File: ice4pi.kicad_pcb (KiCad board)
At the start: 4 copper layers, 85 x 56 mm, 41 parts, among them J1 Conn_02x03, J2 Raspberry_Pi_2_3, J3 USB_C_Receptacle_USB2.0, J4 RJ45_Abracon_ARJP11A-MASA-B-A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, U1 ENC28J60x-SS, U2 DSC1001DE1-025.0000, U3 TPS2375-1

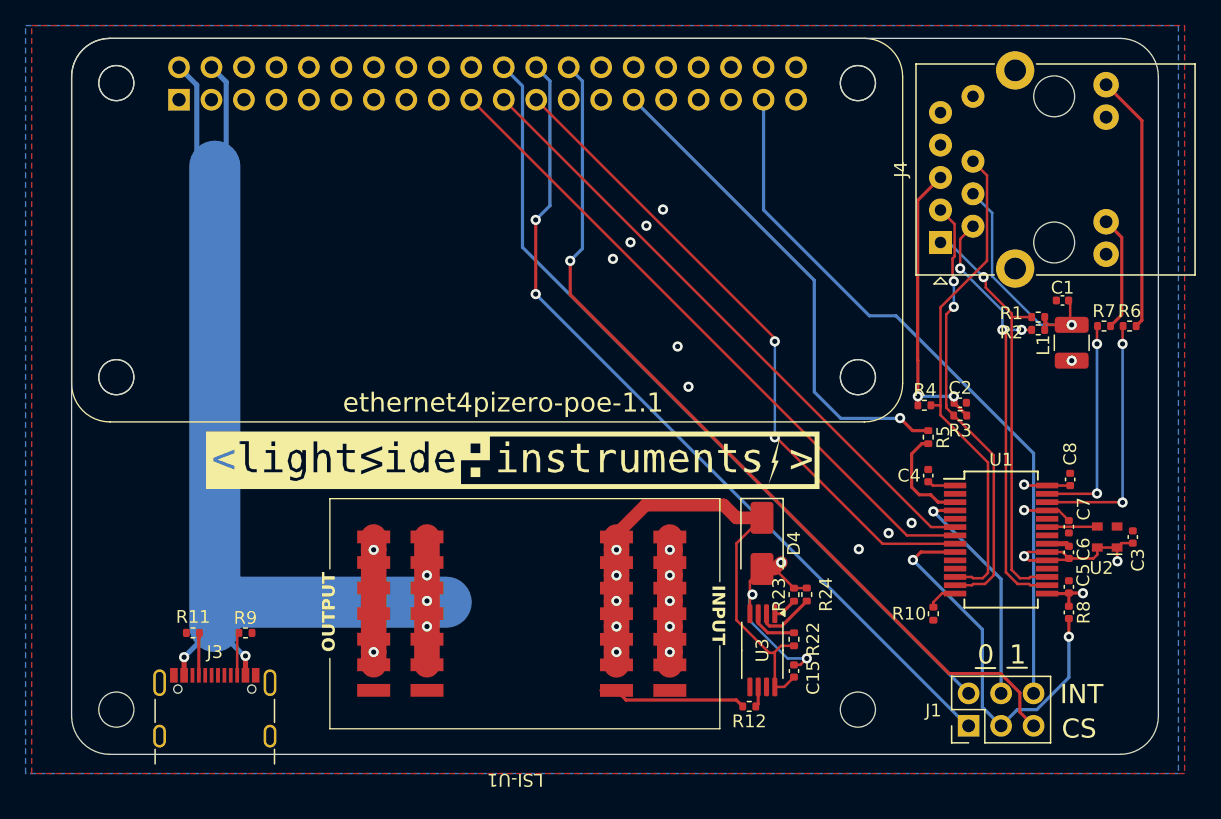
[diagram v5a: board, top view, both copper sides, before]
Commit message: feat: fixed led polarity
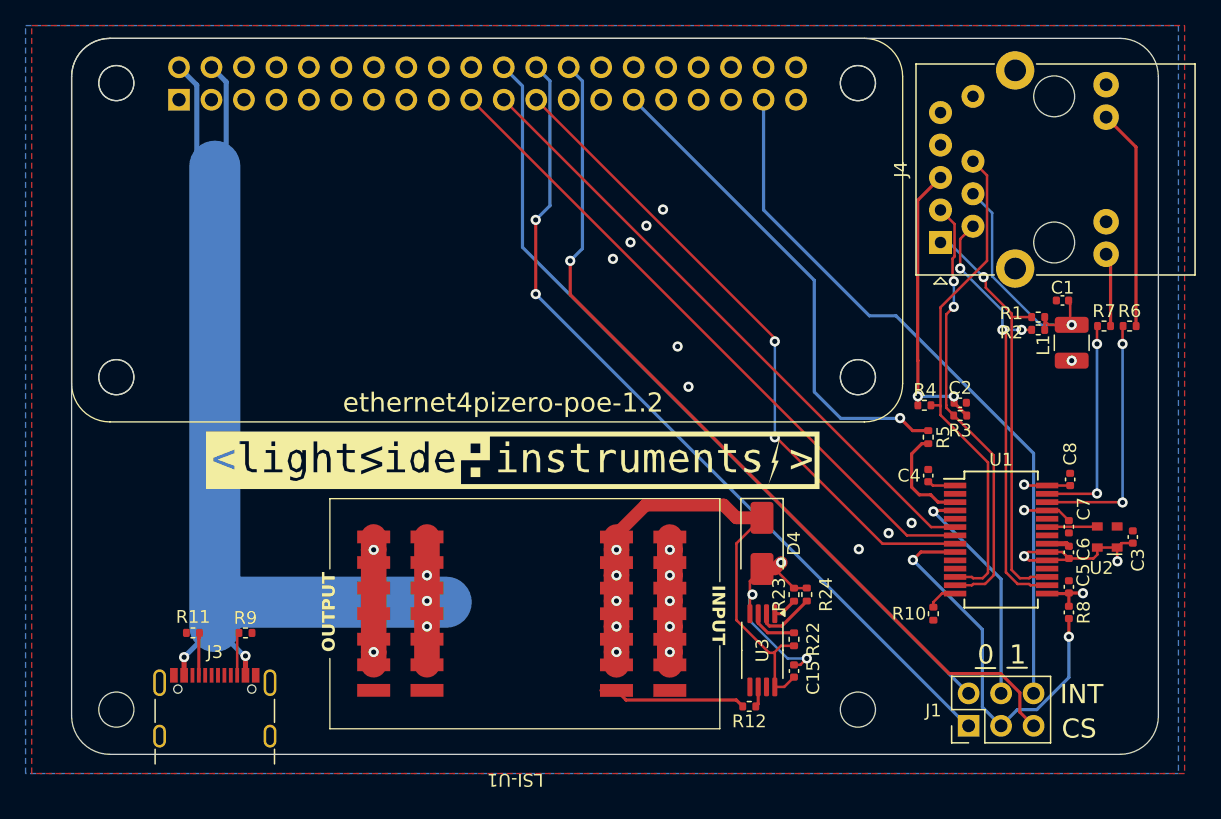
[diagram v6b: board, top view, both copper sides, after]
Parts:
- R12: value 332K -> 0
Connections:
- J4 pad 11: GND -> Net-(J4-Pad11)
- J4 pad 12: Net-(J4-Pad12) -> GND
- J4 pad 13: GND -> Net-(J4-Pad13)
- J4 pad 14: Net-(J4-Pad14) -> GND
- R6 pad 2: Net-(J4-Pad14) -> Net-(J4-Pad13)
- R7 pad 2: Net-(J4-Pad12) -> Net-(J4-Pad11)
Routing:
- net Net-(J4-Pad14): track 21.6 -> 0.00 mm
- net Net-(J4-Pad13): track 0.00 -> 17.3 mm
- net Net-(J4-Pad12): track 9.02 -> 0.00 mm
- net Net-(J4-Pad11): track 0.00 -> 6.42 mm
- net GND: track 22.5 -> 23.3 mm
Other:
- board text added: "ethernet4pizero-poe-1.2"
- board text removed: "ethernet4pizero-poe-1.1"
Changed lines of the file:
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@@
 	(net 67 "unconnected-(J4-Pad7)")
 	(net 68 "Net-(U3-PG)")
-	(net 69 "Net-(J4-Pad14)")
-	(net 70 "Net-(J4-Pad12)")
+	(net 69 "Net-(J4-Pad13)")
+	(net 70 "Net-(J4-Pad11)")
 	(footprint "ice4pi:mount_hole"
 		(locked yes)
@@
 			(layers "F.Cu" "F.Paste" "F.Mask")
 			(roundrect_rratio 0.25)
-			(net 69 "Net-(J4-Pad14)")
+			(net 69 "Net-(J4-Pad13)")
 			(pintype "passive")
 		)
@@
 			(layers "F.Cu" "F.Paste" "F.Mask")
 			(roundrect_rratio 0.25)
-			(net 70 "Net-(J4-Pad12)")
+			(net 70 "Net-(J4-Pad11)")
 			(pintype "passive")
 		)
@@
 			(layers "*.Cu" "*.Mask")
 			(remove_unused_layers no)
-			(net 1 "GND")
+			(net 70 "Net-(J4-Pad11)")
 			(pintype "passive")
 		)
@@
 			(layers "*.Cu" "*.Mask")
 			(remove_unused_layers no)
-			(net 70 "Net-(J4-Pad12)")
+			(net 1 "GND")
 			(pintype "passive")
 		)
@@
 			(layers "*.Cu" "*.Mask")
 			(remove_unused_layers no)
-			(net 1 "GND")
+			(net 69 "Net-(J4-Pad13)")
 			(pintype "passive")
 		)
@@
 			(layers "*.Cu" "*.Mask")
 			(remove_unused_layers no)
-			(net 69 "Net-(J4-Pad14)")
+			(net 1 "GND")
 			(pintype "passive")
 		)
@@
 			)
 		)
-		(property "Value" "332K"
+		(property "Value" "0"
 			(at 0 1.17 0)
 			(layer "F.Fab")
@@
 		(layer "Edge.Cuts")
 	)
-	(gr_text "ethernet4pizero-poe-1.1"
+	(gr_text "ethernet4pizero-poe-1.2"
 		(at 83.75 77.5 0)
 		(layer "F.SilkS")
@@
 	)
 	(segment
-		(start 131.310732 66.285732)
-		(end 130.91 65.885)
-		(width 0.25)
-		(layer "F.Cu")
-		(net 1)
-	)
-	(segment
 		(start 73.625015 87.994762)
 		(end 73.625015 89)
@@
 	)
 	(segment
+		(start 131.556431 52.925)
+		(end 130.22 52.925)
+		(width 0.2)
+		(layer "F.Cu")
+		(net 1)
+	)
+	(segment
 		(start 96.787024 98.001469)
 		(end 96.787024 97)
@@
 	)
 	(segment
-		(start 133.709536 71.050464)
-		(end 133.709536 55.424536)
+		(start 133.25 71.49)
+		(end 133.25 57.505)
 		(width 0.25)
 		(layer "F.Cu")
@@
 	)
 	(segment
-		(start 133.709536 55.424536)
-		(end 130.91 52.625)
+		(start 133.26 71.5)
+		(end 133.25 71.49)
 		(width 0.25)
 		(layer "F.Cu")
@@
 	)
 	(segment
-		(start 131.556431 52.925)
-		(end 130.22 52.925)
-		(width 0.2)
-		(layer "F.Cu")
-		(net 69)
-	)
-	(segment
-		(start 133.26 71.5)
-		(end 133.709536 71.050464)
+		(start 133.25 57.505)
+		(end 130.91 55.165)
 		(width 0.25)
 		(layer "F.Cu")
@@
 	)
 	(segment
-		(start 132.135 70.625)
-		(end 132.135 64.57)
+		(start 131.26 71.5)
+		(end 131.26 66.145)
 		(width 0.25)
 		(layer "F.Cu")
@@
 	)
 	(segment
-		(start 132.135 64.57)
-		(end 130.91 63.345)
+		(start 131.310732 66.285732)
+		(end 130.91 65.885)
 		(width 0.25)
 		(layer "F.Cu")
@@
 	)
 	(segment
-		(start 131.26 71.5)
-		(end 132.135 70.625)
+		(start 131.26 66.145)
+		(end 130.91 65.795)
 		(width 0.25)
 		(layer "F.Cu")
